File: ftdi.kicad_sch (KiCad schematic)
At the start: 31 parts

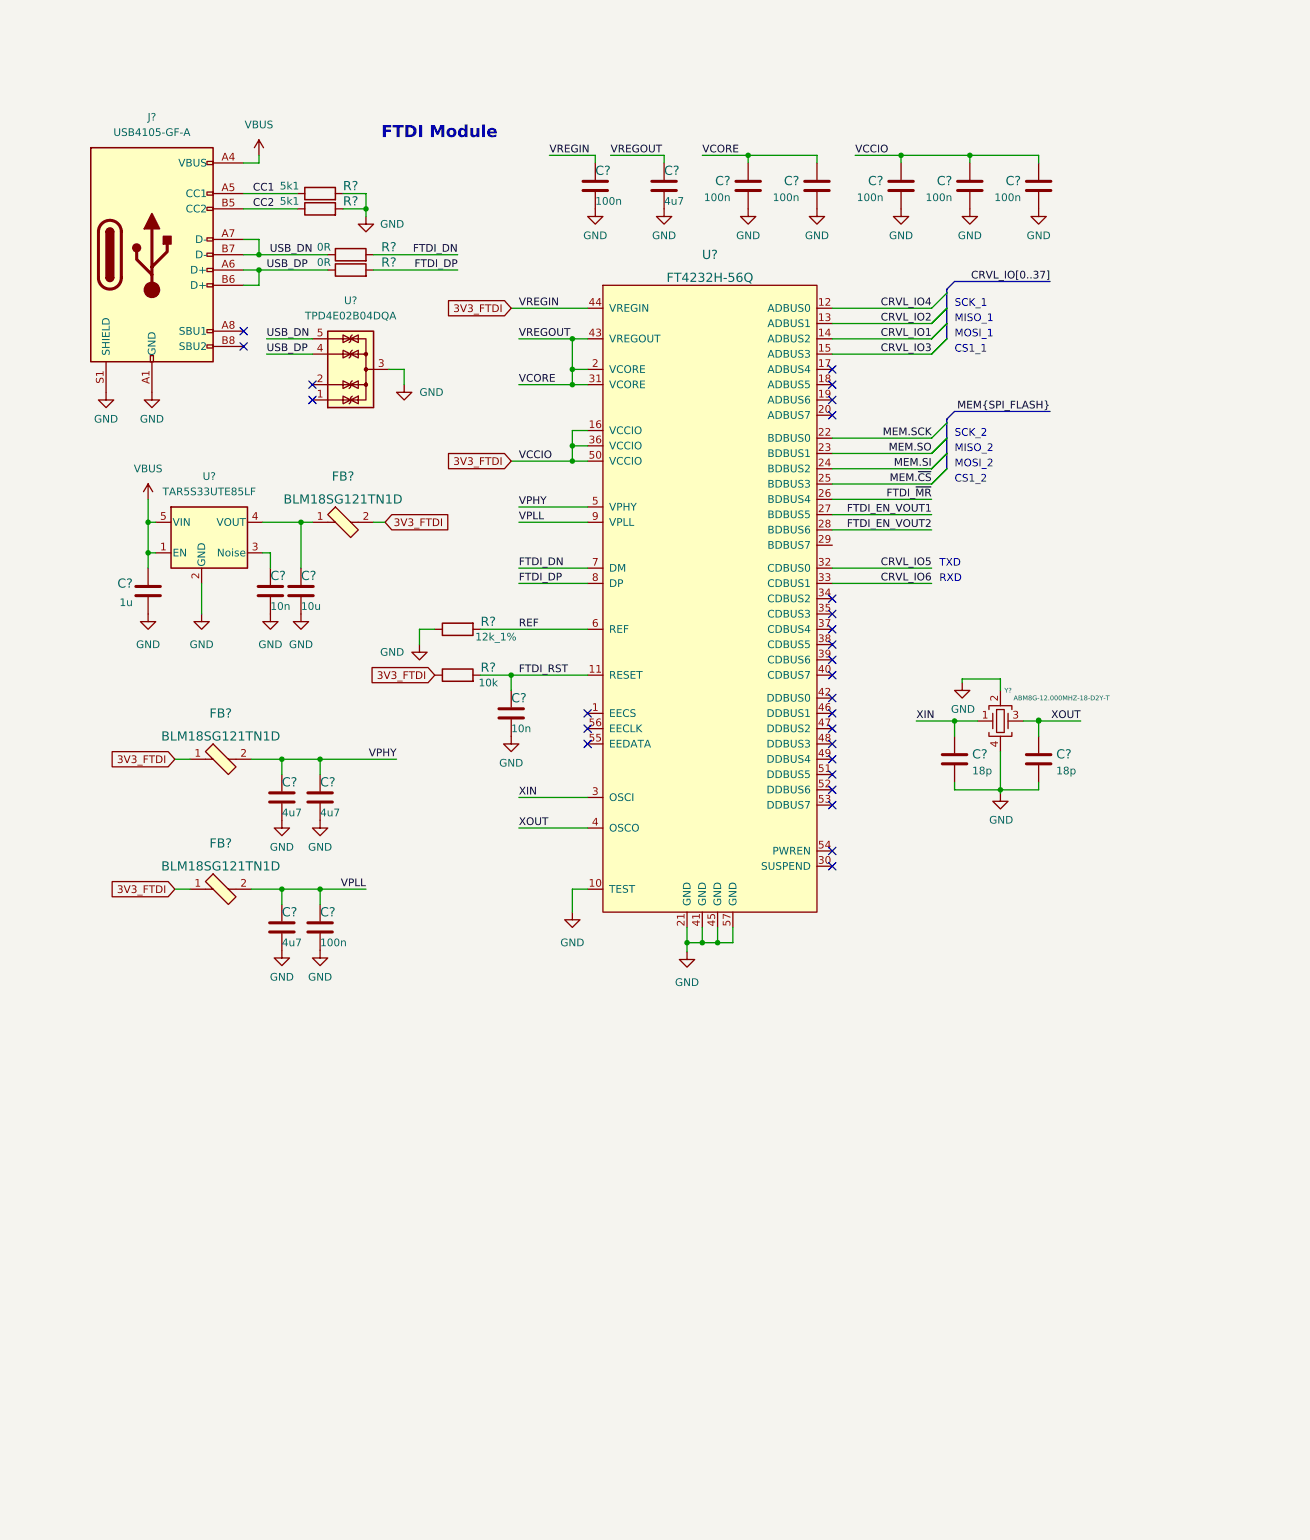
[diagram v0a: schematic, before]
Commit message: Adjusted net naming to work in subsheet
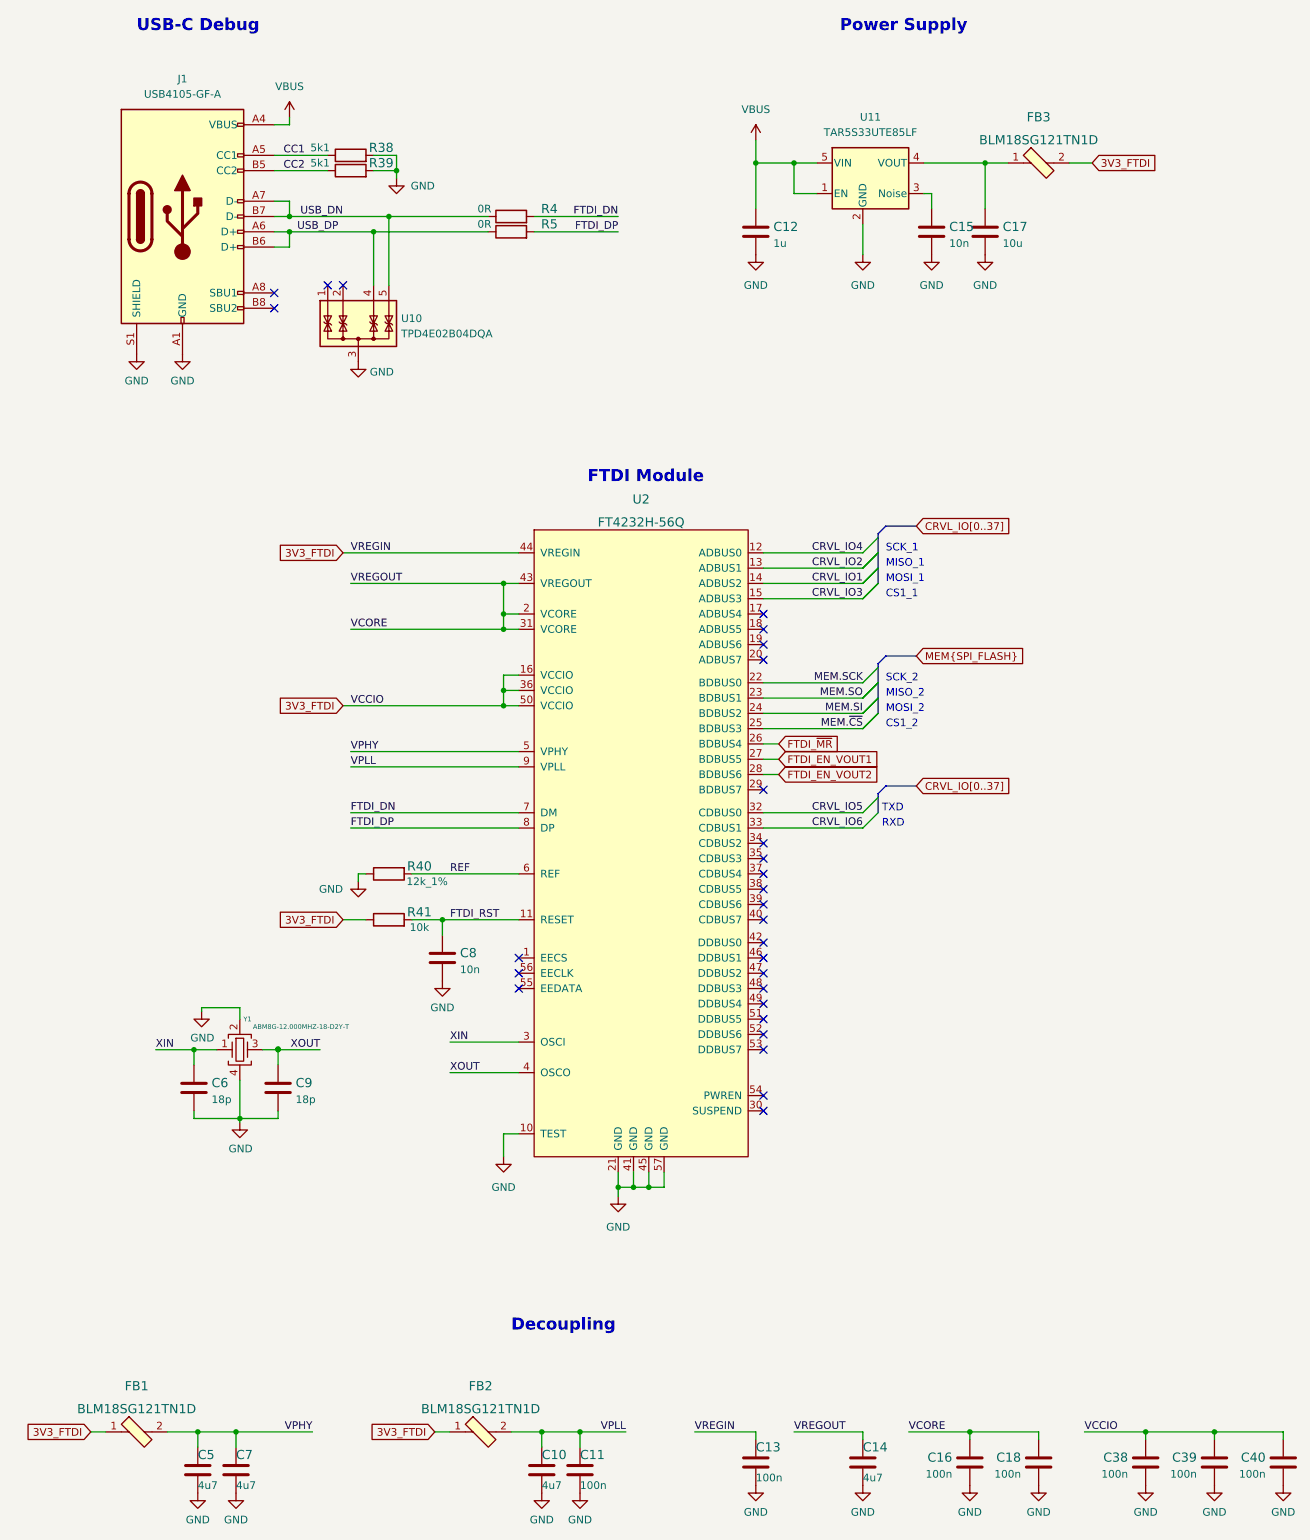
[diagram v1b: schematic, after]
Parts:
- gave numbers to parts that had none: 31
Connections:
- no-connect marks 27 -> 28
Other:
- note added: "Decoupling"
- note added: "Power Supply"
- note added: "USB-C Debug"
- moved on the sheet: C10, C11, C12, C13, C14, C15, C16, C17, C18, C38, C39, C40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

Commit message: Imported all changes to PCB. Cleared old tracks. Started placement and layout
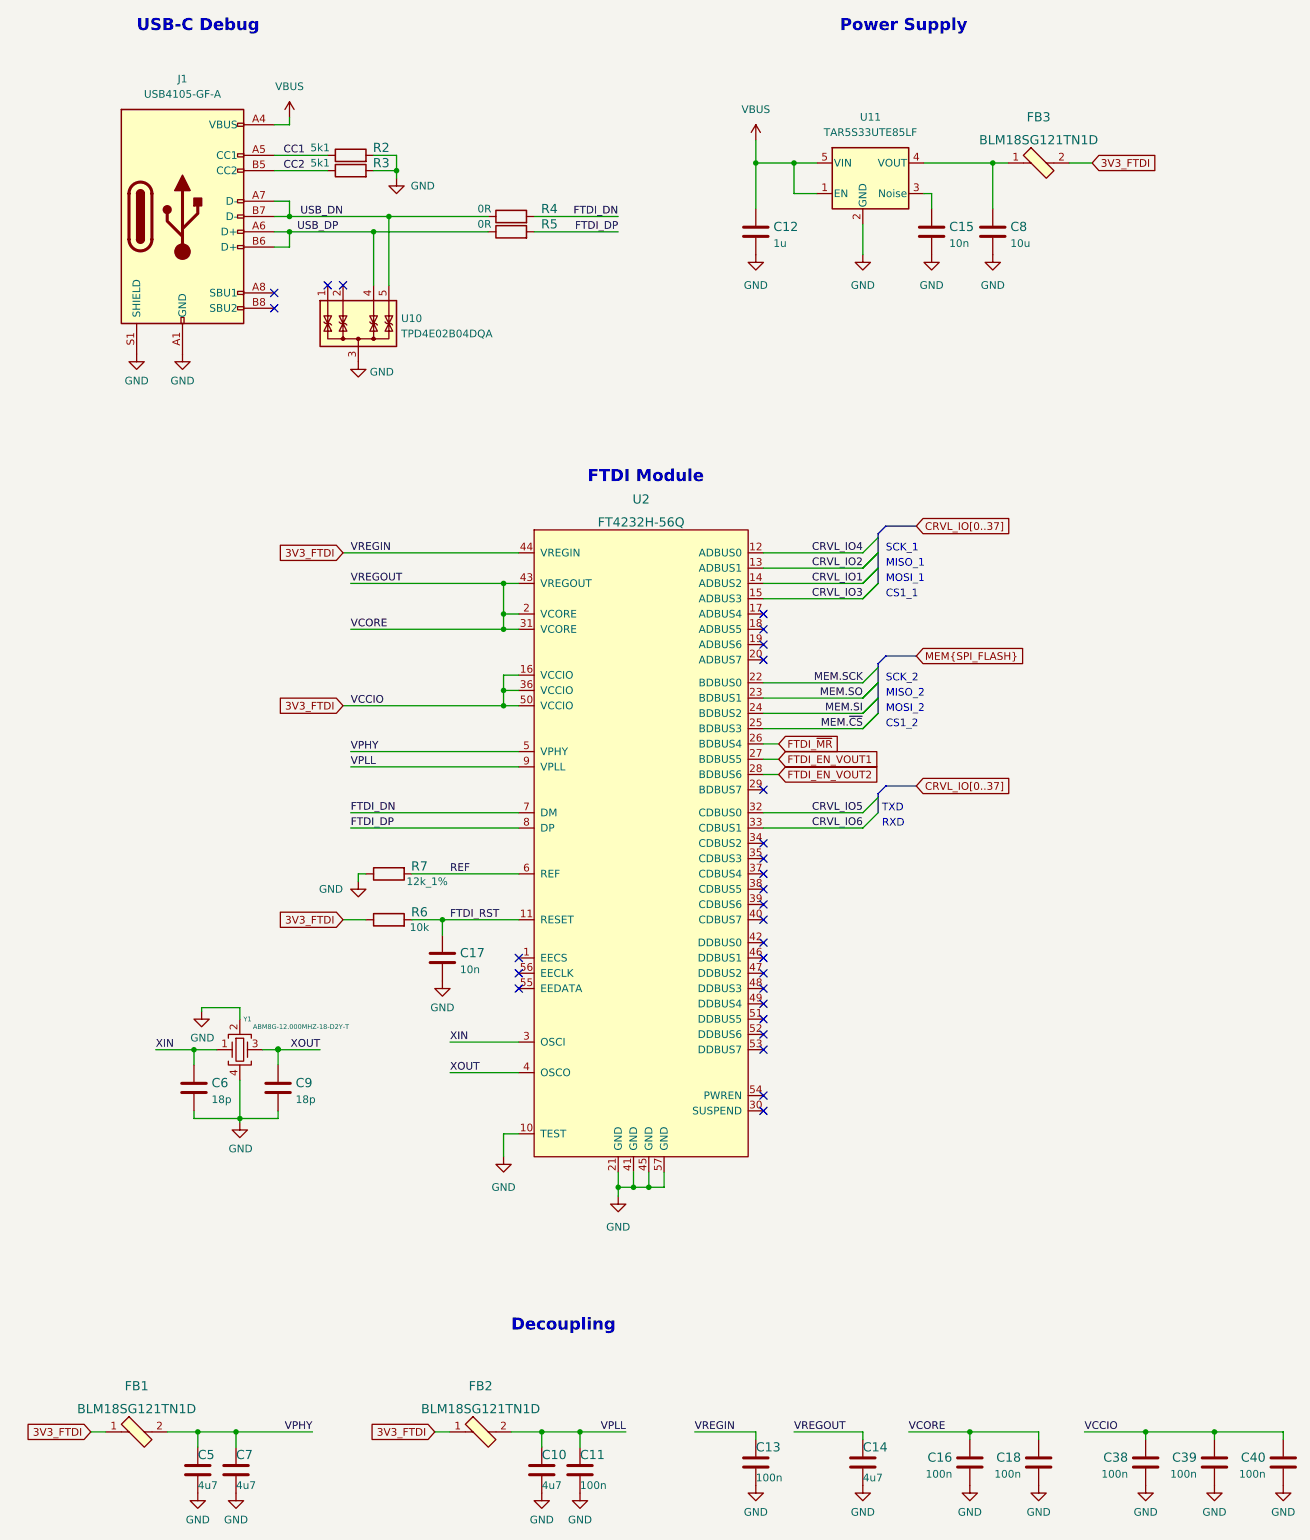
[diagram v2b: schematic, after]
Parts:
- renumbered C8 to C17, C17 to C8, R38 to R2, R39 to R3, R41 to R6, R40 to R7
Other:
- moved on the sheet: C8
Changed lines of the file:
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@@
   (junction (at 149.86 48.26) (diameter 0) (color 0 0 0 0)
   )
+  (junction (at 182.88 48.26) (diameter 0) (color 0 0 0 0)
+  )
   (junction (at 219.71 259.08) (diameter 0) (color 0 0 0 0)
   )
@@
   )
   (junction (at 120.65 218.44) (diameter 0) (color 0 0 0 0)
-  )
-  (junction (at 181.61 48.26) (diameter 0) (color 0 0 0 0)
   )
   (no_connect (at 144.78 128.27))
@@
     (stroke (width 0) (type default) (color 0 0 0 0))
   )
-  (wire (pts (xy 171.45 48.26) (xy 181.61 48.26))
-    (stroke (width 0) (type default) (color 0 0 0 0))
-  )
   (wire (pts (xy 128.27 218.44) (xy 125.73 218.44))
     (stroke (width 0) (type default) (color 0 0 0 0))
@@
     (stroke (width 0) (type default) (color 0 0 0 0))
   )
+  (wire (pts (xy 182.88 48.26) (xy 185.42 48.26))
+    (stroke (width 0) (type default) (color 0 0 0 0))
+  )
   (wire (pts (xy 76.2 125.73) (xy 101.6 125.73))
     (stroke (width 0) (type default) (color 0 0 0 0))
@@
     (stroke (width 0) (type default) (color 0 0 0 0))
   )
-  (wire (pts (xy 181.61 48.26) (xy 185.42 48.26))
-    (stroke (width 0) (type default) (color 0 0 0 0))
-  )
   (wire (pts (xy 80.01 49.53) (xy 83.82 49.53))
     (stroke (width 0) (type default) (color 0 0 0 0))
@@
     (stroke (width 0) (type default) (color 0 0 0 0))
   )
-  (wire (pts (xy 181.61 48.26) (xy 181.61 55.88))
+  (wire (pts (xy 182.88 48.26) (xy 182.88 55.88))
     (stroke (width 0) (type default) (color 0 0 0 0))
   )
   (wire (pts (xy 101.6 125.73) (xy 101.6 123.19))
+    (stroke (width 0) (type default) (color 0 0 0 0))
+  )
+  (wire (pts (xy 171.45 48.26) (xy 182.88 48.26))
     (stroke (width 0) (type default) (color 0 0 0 0))
   )
@@
     (pin "2")
   )
-  (symbol (lib_id "arty-mpw-tester:GND") (at 181.61 63.5 0) (mirror y) (unit 1)
-    (in_bom yes) (on_board yes) (fields_autoplaced)
-    (property "Reference" "#PWR029" (id 0) (at 181.61 69.85 0)
-      (effects (font (size 1.27 1.27)) hide)
-    )
-    (property "Value" "GND" (id 1) (at 181.61 68.58 0))
-    (property "Footprint" "" (id 2) (at 181.61 63.5 0)
-      (effects (font (size 1.27 1.27)) hide)
-    )
-    (property "Datasheet" "" (id 3) (at 181.61 63.5 0)
+  (symbol (lib_id "arty-mpw-tester:GND") (at 182.88 63.5 0) (mirror y) (unit 1)
+    (in_bom yes) (on_board yes) (fields_autoplaced)
+    (property "Reference" "#PWR029" (id 0) (at 182.88 69.85 0)
+      (effects (font (size 1.27 1.27)) hide)
+    )
+    (property "Value" "GND" (id 1) (at 182.88 68.58 0))
+    (property "Footprint" "" (id 2) (at 182.88 63.5 0)
+      (effects (font (size 1.27 1.27)) hide)
+    )
+    (property "Datasheet" "" (id 3) (at 182.88 63.5 0)
       (effects (font (size 1.27 1.27)) hide)
     )
@@
   (symbol (lib_id "arty-mpw-tester:C_10n_0603") (at 91.44 180.34 0) (unit 1)
     (in_bom yes) (on_board yes) (fields_autoplaced)
-    (property "Reference" "C8" (id 0) (at 94.361 179.5054 0)
+    (property "Reference" "C17" (id 0) (at 94.361 179.5054 0)
       (effects (font (size 1.524 1.524)) (justify left))
     )
@@
   (symbol (lib_id "arty-mpw-tester:R_5k1_0603") (at 76.2 49.53 0) (unit 1)
     (in_bom yes) (on_board yes)
-    (property "Reference" "R39" (id 0) (at 81.28 48.26 0)
+    (property "Reference" "R3" (id 0) (at 81.28 48.26 0)
       (effects (font (size 1.524 1.524)))
     )
@@
   (symbol (lib_id "arty-mpw-tester:R_12k_1%_0603") (at 82.55 166.37 0) (mirror x) (unit 1)
     (in_bom yes) (on_board yes)
-    (property "Reference" "R40" (id 0) (at 87.63 165.1 0)
+    (property "Reference" "R7" (id 0) (at 87.63 165.1 0)
       (effects (font (size 1.524 1.524)))
     )
@@
   (symbol (lib_id "arty-mpw-tester:R_10k_0603") (at 82.55 173.99 0) (unit 1)
     (in_bom yes) (on_board yes)
-    (property "Reference" "R41" (id 0) (at 87.63 172.72 0)
+    (property "Reference" "R6" (id 0) (at 87.63 172.72 0)
       (effects (font (size 1.524 1.524)))
     )
@@
     (pin "4")
   )
-  (symbol (lib_id "antmicroCapacitors0603:C_10u_0603") (at 181.61 59.69 0) (unit 1)
-    (in_bom yes) (on_board yes) (fields_autoplaced)
-    (property "Reference" "C17" (id 0) (at 184.531 58.8554 0)
+  (symbol (lib_id "antmicroCapacitors0603:C_10u_0603") (at 182.88 59.69 0) (unit 1)
+    (in_bom yes) (on_board yes) (fields_autoplaced)
+    (property "Reference" "C8" (id 0) (at 185.801 58.8554 0)
       (effects (font (size 1.524 1.524)) (justify left))
     )
-    (property "Value" "C_10u_0603" (id 1) (at 181.61 63.5 0)
-      (effects (font (size 1.524 1.524)) hide)
-    )
-    (property "Footprint" "antmicro-footprints:0603-cap" (id 2) (at 186.69 54.61 0)
-      (effects (font (size 1.524 1.524)) (justify left) hide)
-    )
-    (property "Datasheet" "" (id 3) (at 181.61 59.69 0)
-      (effects (font (size 1.27 1.27)) hide)
-    )
-    (property "Manufacturer" "Murata" (id 4) (at 186.69 49.53 0)
-      (effects (font (size 1.524 1.524)) (justify left) hide)
-    )
-    (property "MPN" "GRM188R61A106KE69D" (id 5) (at 186.69 52.07 0)
-      (effects (font (size 1.524 1.524)) (justify left) hide)
-    )
-    (property "Val" "10u" (id 6) (at 184.531 61.6205 0)
+    (property "Value" "C_10u_0603" (id 1) (at 182.88 63.5 0)
+      (effects (font (size 1.524 1.524)) hide)
+    )
+    (property "Footprint" "antmicro-footprints:0603-cap" (id 2) (at 187.96 54.61 0)
+      (effects (font (size 1.524 1.524)) (justify left) hide)
+    )
+    (property "Datasheet" "" (id 3) (at 182.88 59.69 0)
+      (effects (font (size 1.27 1.27)) hide)
+    )
+    (property "Manufacturer" "Murata" (id 4) (at 187.96 49.53 0)
+      (effects (font (size 1.524 1.524)) (justify left) hide)
+    )
+    (property "MPN" "GRM188R61A106KE69D" (id 5) (at 187.96 52.07 0)
+      (effects (font (size 1.524 1.524)) (justify left) hide)
+    )
+    (property "Val" "10u" (id 6) (at 185.801 61.6205 0)
       (effects (font (size 1.27 1.27)) (justify left))
     )
@@
   (symbol (lib_id "arty-mpw-tester:R_5k1_0603") (at 76.2 46.99 0) (unit 1)
     (in_bom yes) (on_board yes)
-    (property "Reference" "R38" (id 0) (at 81.28 45.72 0)
+    (property "Reference" "R2" (id 0) (at 81.28 45.72 0)
       (effects (font (size 1.524 1.524)))
     )

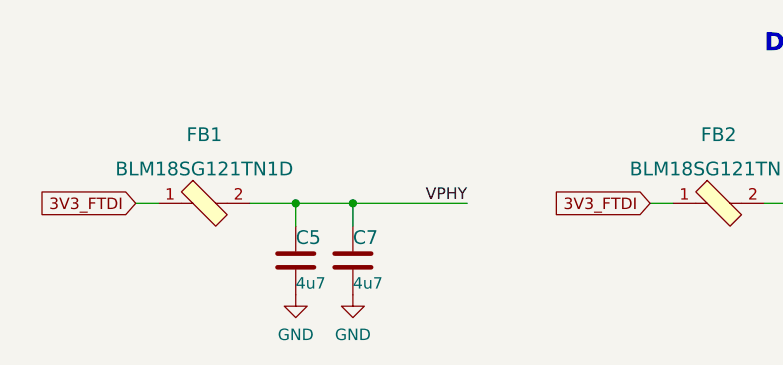
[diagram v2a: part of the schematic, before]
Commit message: Finished initial routing. Corrected switch footprint
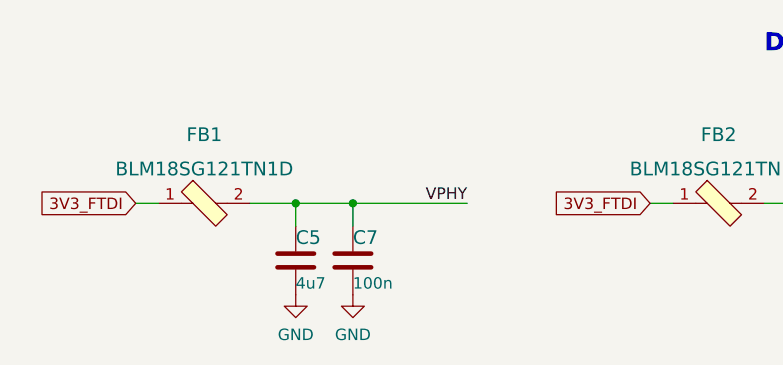
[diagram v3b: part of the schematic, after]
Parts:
- removed C7: C_4u7_0603, arty-mpw-tester-footprints:0603-cap, symbol arty-mpw-tester:C_4u7_0603
- added C7: C_100n_0603, arty-mpw-tester-footprints:0603-cap, symbol arty-mpw-tester:C_100n_0603
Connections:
- net GND: now also C7.2
- net VPHY: now also C7.1
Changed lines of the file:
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@@
     (pin "1")
+  )
+  (symbol (lib_id "arty-mpw-tester:C_100n_0603") (at 57.15 265.43 0) (unit 1)
+    (in_bom yes) (on_board yes)
+    (property "Reference" "C7" (id 0) (at 57.15 262.89 0)
+      (effects (font (size 1.524 1.524)) (justify left))
+    )
+    (property "Value" "C_100n_0603" (id 1) (at 57.15 269.24 0)
+      (effects (font (size 1.524 1.524)) hide)
+    )
+    (property "Footprint" "arty-mpw-tester-footprints:0603-cap" (id 2) (at 62.23 260.35 0)
+      (effects (font (size 1.524 1.524)) (justify left) hide)
+    )
+    (property "Datasheet" "" (id 3) (at 57.15 265.43 0)
+      (effects (font (size 1.27 1.27)) hide)
+    )
+    (property "Manufacturer" "AVX" (id 4) (at 62.23 255.27 0)
+      (effects (font (size 1.524 1.524)) (justify left) hide)
+    )
+    (property "MPN" "0603YC104KAZ2A" (id 5) (at 62.23 257.81 0)
+      (effects (font (size 1.524 1.524)) (justify left) hide)
+    )
+    (property "Val" "100n" (id 6) (at 57.15 267.97 0)
+      (effects (font (size 1.27 1.27)) (justify left))
+    )
+    (pin "1")
+    (pin "2")
   )
   (symbol (lib_id "arty-mpw-tester:R_0R_0402") (at 102.87 57.15 0) (unit 1)
@@
     (pin "9")
   )
-  (symbol (lib_id "arty-mpw-tester:C_4u7_0603") (at 57.15 265.43 0) (unit 1)
-    (in_bom yes) (on_board yes)
-    (property "Reference" "C7" (id 0) (at 57.15 262.89 0)
-      (effects (font (size 1.524 1.524)) (justify left))
-    )
-    (property "Value" "C_4u7_0603" (id 1) (at 57.15 269.24 0)
-      (effects (font (size 1.524 1.524)) hide)
-    )
-    (property "Footprint" "arty-mpw-tester-footprints:0603-cap" (id 2) (at 62.23 260.35 0)
-      (effects (font (size 1.524 1.524)) (justify left) hide)
-    )
-    (property "Datasheet" "" (id 3) (at 57.15 265.43 0)
-      (effects (font (size 1.27 1.27)) hide)
-    )
-    (property "Manufacturer" "TDK" (id 4) (at 62.23 255.27 0)
-      (effects (font (size 1.524 1.524)) (justify left) hide)
-    )
-    (property "MPN" "C1608X5R1V475M080AC" (id 5) (at 62.23 257.81 0)
-      (effects (font (size 1.524 1.524)) (justify left) hide)
-    )
-    (property "Val" "4u7" (id 6) (at 57.15 267.97 0)
-      (effects (font (size 1.27 1.27)) (justify left))
-    )
-    (pin "1")
-    (pin "2")
-  )
   (symbol (lib_id "arty-mpw-tester:C_1u_0603") (at 143.51 59.69 0) (unit 1)
